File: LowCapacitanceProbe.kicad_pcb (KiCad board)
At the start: 4 copper layers, 25.7 x 19.4 mm, 41 parts, among them J2 OUTPUT, J3 POWER IN, Q1 BF998, U2 SPX3819M5-L-5-0

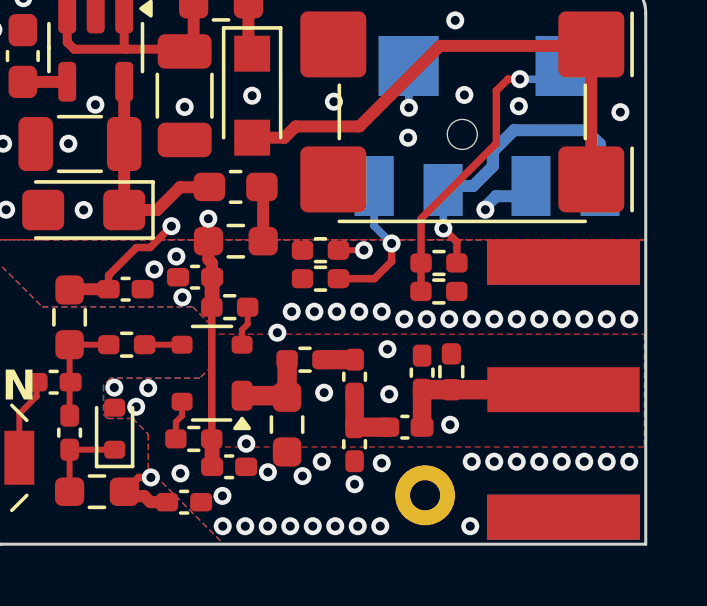
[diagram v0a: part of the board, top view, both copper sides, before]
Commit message: Fixed some RF traces, copper fills, added some teardrops.
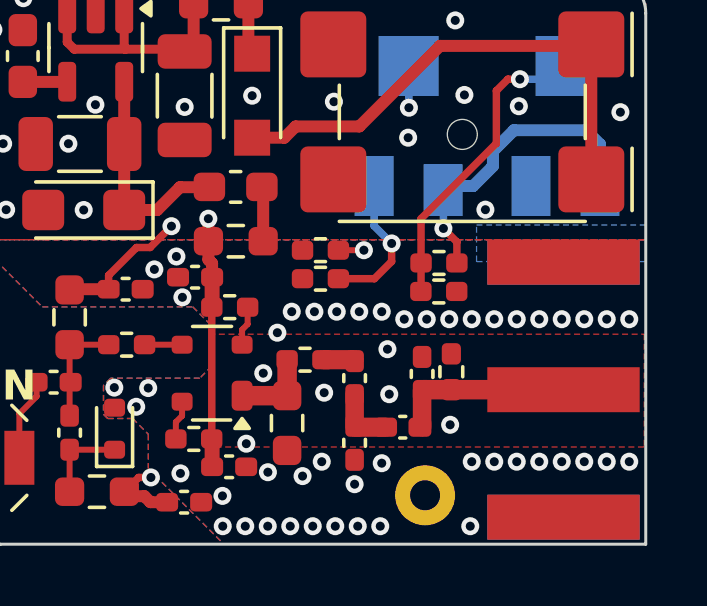
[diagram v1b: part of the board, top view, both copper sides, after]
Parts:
- moved L1 0.07 mm to (110.8, 73.7)
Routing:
- net GND: track 8.92 -> 7.13 mm, vias 77 -> 78

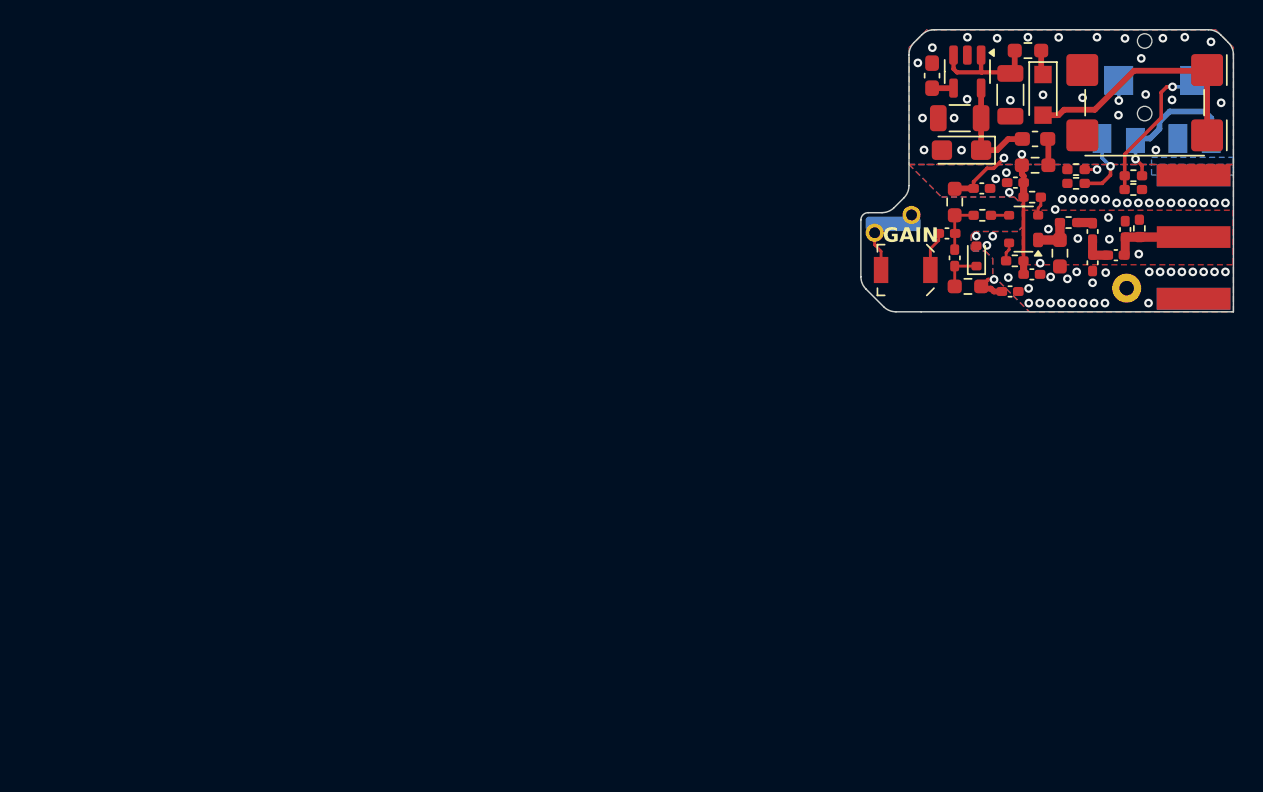
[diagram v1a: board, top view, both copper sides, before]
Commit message: Some more fixes to GND fill, added board stackup and board characteristics.
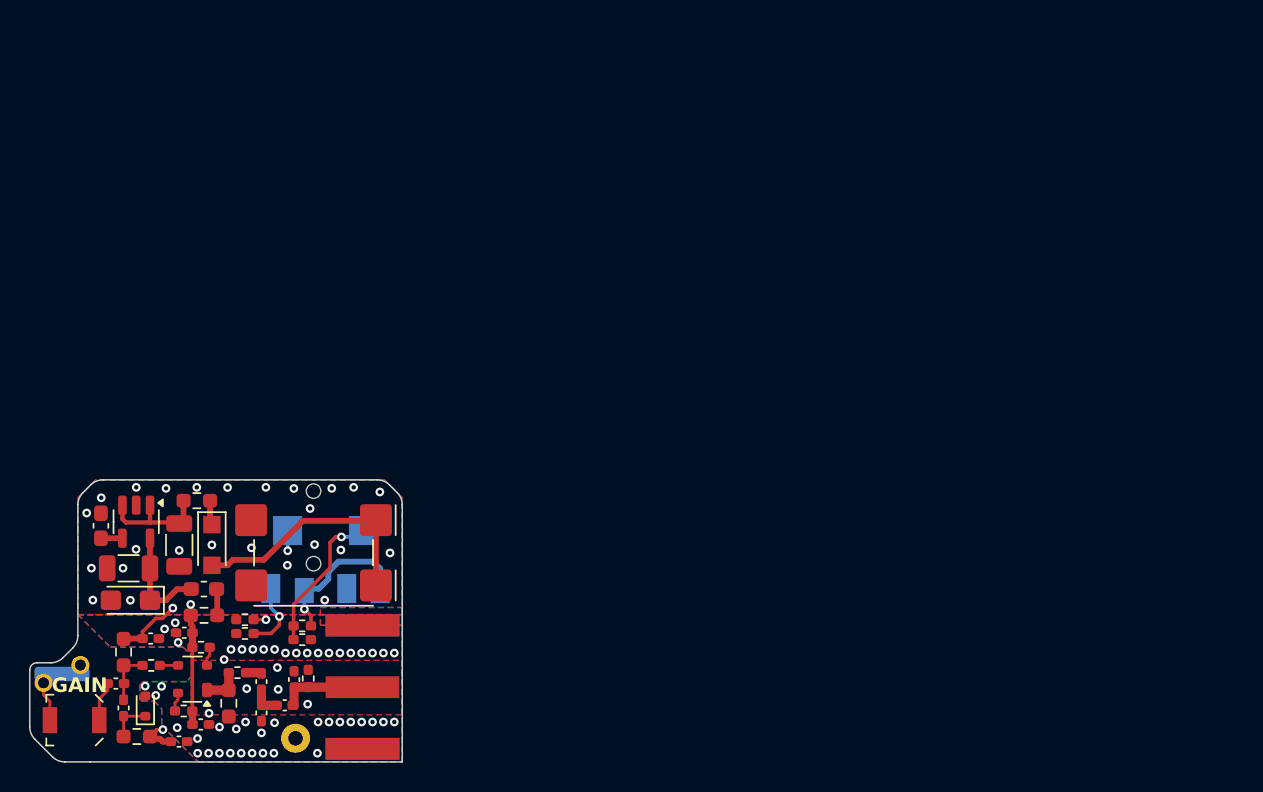
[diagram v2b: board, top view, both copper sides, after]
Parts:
- moved C1 65.1 mm to (42.7, 95.3)
- moved C11 65.1 mm to (42.4, 104.9)
- moved C12 65.1 mm to (46.2, 107.2)
- moved C13 65.1 mm to (40.8, 92.4)
- moved C14 65.1 mm to (47.7, 106.1)
- moved C3 65.1 mm to (41.8, 103.2)
- moved C5 65.1 mm to (51.9, 103.1)
- moved C7 65.1 mm to (54.1, 103.0)
- moved C8 65.1 mm to (42.9, 97.5)
- moved C9 65.1 mm to (39.0, 105.8)
- moved D1 65.1 mm to (43.9, 104.8)
- moved FB1 65.1 mm to (47.9, 96.7)
- moved J2 65.1 mm to (58.8, 103.5)
- moved R10 65.1 mm to (49.6, 104.6)
- moved R11 65.1 mm to (54.7, 99.3)
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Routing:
- net GND: vias 78 -> 77
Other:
- board text added: "0"
- board text added: "0 mm"
- board text added: "0.0152 mm"
- board text added: "0.01524 mm"
- board text added: "0.02"
- board text added: "0.035 mm"
- board text added: "0.0994 mm"
- board text added: "0.1000 mm / 0.1000 mm"
- board text added: "0.3000 mm"
- board text added: "1"
- board text added: "1.265 mm"
- board text added: "1.5947 mm"
- board text added: "25.6700 mm x 19.4350 mm"
- board text added: "3.8"
- board text added: "4"
- board text added: "4.1"
- board text added: "4.43"
- board text added: "B.Cu"
- board text added: "B.Mask"
- board text added: "B.Paste"
- board text added: "B.Silkscreen"
- board text added: "BOARD CHARACTERISTICS"
- board text added: "Board Thickness:"
- board text added: "Board overall dimensions:"
- board text added: "Bottom Silk Screen"
- board text added: "Bottom Solder Mask"
- board text added: "Bottom Solder Paste"
- board text added: "Castellated pads:"
- board text added: "Color"
- board text added: "Copper Finish:"
- board text added: "Copper Layer Count:"
- board text added: "Dielectric"
- board text added: "ENIG"
- board text added: "Edge card connectors:"
- board text added: "Epsilon R"
- board text added: "F.Cu"
- board text added: "F.Mask"
- board text added: "F.Paste"
- board text added: "F.Silkscreen"
- board text added: "FR4 natural"
- board text added: "Impedance Control:"
- board text added: "In1.Cu"
- board text added: "In2.Cu"
- board text added: "JLCPCB Soldermask"
- board text added: "Layer Name"
- board text added: "Loss Tangent"
- board text added: "Material"
- board text added: "Min hole diameter:"
- board text added: "Min track/spacing:"
- board text added: "Nan Ya Plastics NP-155F 3313"
- board text added: "Nan Ya Plastics NP-155F Core"
- board text added: "No"
- board text added: "Not specified"
- board text added: "Plated Board Edge:"
- board text added: "Thickness (mm)"
- board text added: "Top Silk Screen"
- board text added: "Top Solder Mask"
- board text added: "Top Solder Paste"
- board text added: "Type"
- board text added: "Yes"
- board text added: "copper"
- board text added: "core"
- board text added: "prepreg"
